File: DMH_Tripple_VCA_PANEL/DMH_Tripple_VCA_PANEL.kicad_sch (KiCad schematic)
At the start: 21 parts, among them J0 Panel_GND_Solder_Wire_Pad

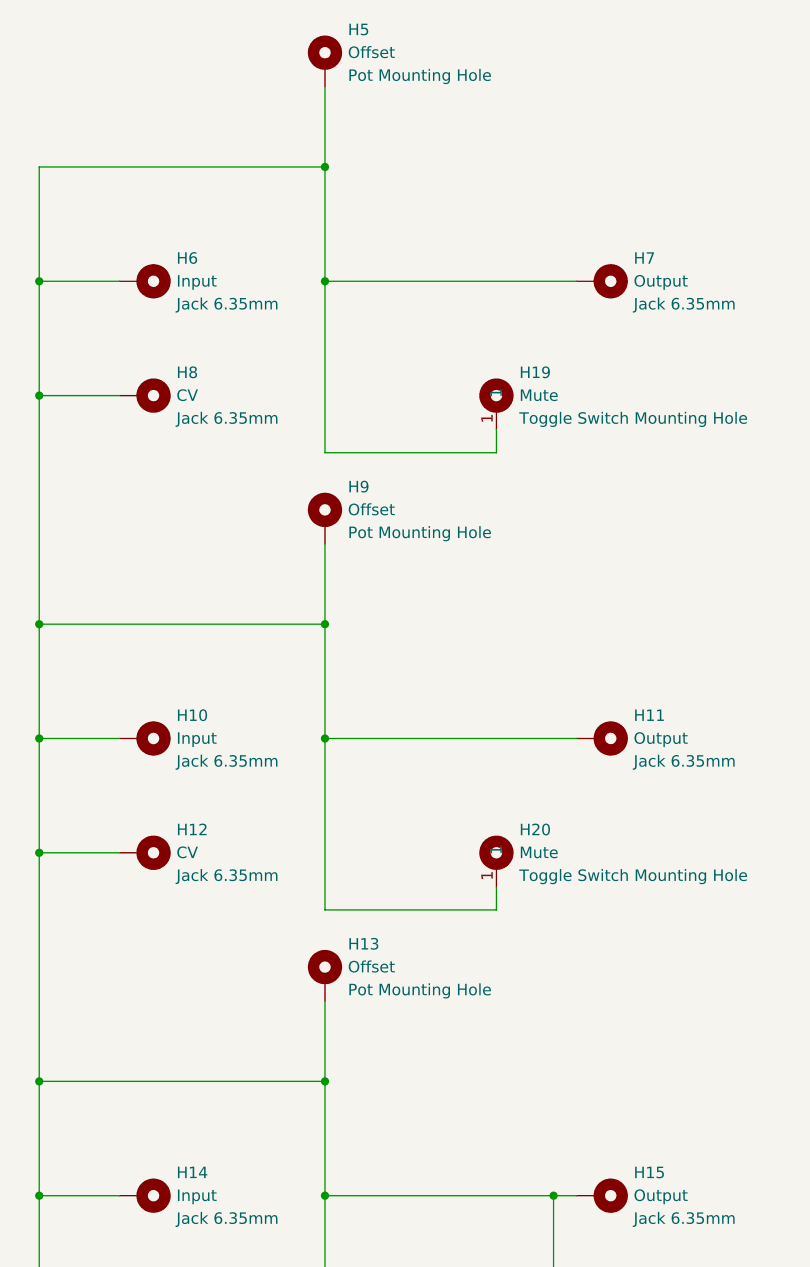
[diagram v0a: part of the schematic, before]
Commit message: Added LED holes
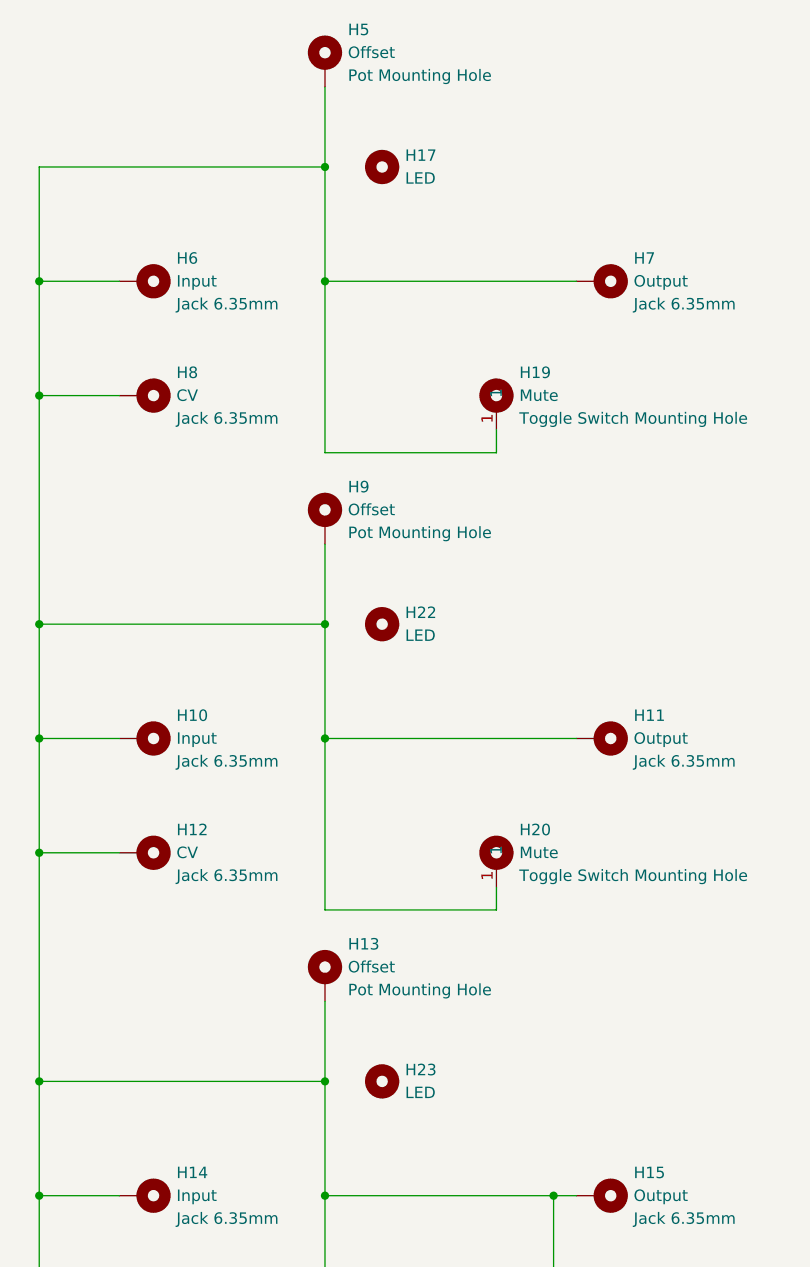
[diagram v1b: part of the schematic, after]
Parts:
- added H17, H22, H23: LED, SynthStuff:MountingHole_LED_3mm, symbol Mechanical:MountingHole
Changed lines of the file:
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@@
+	)
+	(symbol
+		(lib_id "Mechanical:MountingHole")
+		(at 88.9 114.3 0)
+		(unit 1)
+		(exclude_from_sim yes)
+		(in_bom no)
+		(on_board yes)
+		(dnp no)
+		(fields_autoplaced yes)
+		(property "Reference" "H22"
+			(at 91.44 113.0299 0)
+			(effects
+				(font
+					(size 1.27 1.27)
+				)
+				(justify left)
+			)
+		)
+		(property "Value" "LED"
+			(at 91.44 115.5699 0)
+			(effects
+				(font
+					(size 1.27 1.27)
+				)
+				(justify left)
+			)
+		)
+		(property "Footprint" "SynthStuff:MountingHole_LED_3mm"
+			(at 88.9 114.3 0)
+			(effects
+				(font
+					(size 1.27 1.27)
+				)
+				(hide yes)
+			)
+		)
+		(property "Datasheet" "~"
+			(at 88.9 114.3 0)
+			(effects
+				(font
+					(size 1.27 1.27)
+				)
+				(hide yes)
+			)
+		)
+		(property "Description" "Mounting Hole without connection"
+			(at 88.9 114.3 0)
+			(effects
+				(font
+					(size 1.27 1.27)
+				)
+				(hide yes)
+			)
+		)
+		(instances
+			(project "DMH_Tripple_VCA_PANEL"
+				(path "/a552705f-a9fe-462e-9913-5cfcc08b233c"
+					(reference "H22")
+					(unit 1)
+				)
+			)
+		)
 	)
 	(symbol
@@
 	)
 	(symbol
+		(lib_id "Mechanical:MountingHole")
+		(at 88.9 63.5 0)
+		(unit 1)
+		(exclude_from_sim yes)
+		(in_bom no)
+		(on_board yes)
+		(dnp no)
+		(fields_autoplaced yes)
+		(property "Reference" "H17"
+			(at 91.44 62.2299 0)
+			(effects
+				(font
+					(size 1.27 1.27)
+				)
+				(justify left)
+			)
+		)
+		(property "Value" "LED"
+			(at 91.44 64.7699 0)
+			(effects
+				(font
+					(size 1.27 1.27)
+				)
+				(justify left)
+			)
+		)
+		(property "Footprint" "SynthStuff:MountingHole_LED_3mm"
+			(at 88.9 63.5 0)
+			(effects
+				(font
+					(size 1.27 1.27)
+				)
+				(hide yes)
+			)
+		)
+		(property "Datasheet" "~"
+			(at 88.9 63.5 0)
+			(effects
+				(font
+					(size 1.27 1.27)
+				)
+				(hide yes)
+			)
+		)
+		(property "Description" "Mounting Hole without connection"
+			(at 88.9 63.5 0)
+			(effects
+				(font
+					(size 1.27 1.27)
+				)
+				(hide yes)
+			)
+		)
+		(instances
+			(project "DMH_Tripple_VCA_PANEL"
+				(path "/a552705f-a9fe-462e-9913-5cfcc08b233c"
+					(reference "H17")
+					(unit 1)
+				)
+			)
+		)
+	)
+	(symbol
 		(lib_id "SynthStuff:MountingHole_Rails")
 		(at 27.94 265.43 0)
@@
 					(unit 1)
 				)
+			)
+		)
+	)
+	(symbol
+		(lib_id "Mechanical:MountingHole")
+		(at 88.9 165.1 0)
+		(unit 1)
+		(exclude_from_sim yes)
+		(in_bom no)
+		(on_board yes)
+		(dnp no)
+		(fields_autoplaced yes)
+		(property "Reference" "H23"
+			(at 91.44 163.8299 0)
+			(effects
+				(font
+					(size 1.27 1.27)
+				)
+				(justify left)
+			)
+		)
+		(property "Value" "LED"
+			(at 91.44 166.3699 0)
+			(effects
+				(font
+					(size 1.27 1.27)
+				)
+				(justify left)
+			)
+		)
+		(property "Footprint" "SynthStuff:MountingHole_LED_3mm"
+			(at 88.9 165.1 0)
+			(effects
+				(font
+					(size 1.27 1.27)
+				)
+				(hide yes)
+			)
+		)
+		(property "Datasheet" "~"
+			(at 88.9 165.1 0)
+			(effects
+				(font
+					(size 1.27 1.27)
+				)
+				(hide yes)
+			)
+		)
+		(property "Description" "Mounting Hole without connection"
+			(at 88.9 165.1 0)
+			(effects
+				(font
+					(size 1.27 1.27)
+				)
+				(hide yes)
+			)
+		)
+		(instances
+			(project "DMH_Tripple_VCA_PANEL"
+				(path "/a552705f-a9fe-462e-9913-5cfcc08b233c"
+					(reference "H23")
+					(unit 1)
+				)

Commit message: Finished Schematic
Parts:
- H17, H22, H23: footprint SynthStuff:MountingHole_LED_3mm -> SynthStuff:MountingHole_LED_5mm
- H18: value Mix Out + -> Mix Out
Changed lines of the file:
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@@
 			)
 		)
-		(property "Footprint" "SynthStuff:MountingHole_LED_3mm"
+		(property "Footprint" "SynthStuff:MountingHole_LED_5mm"
 			(at 88.9 114.3 0)
 			(effects
@@
 			)
 		)
-		(property "Footprint" "SynthStuff:MountingHole_LED_3mm"
+		(property "Footprint" "SynthStuff:MountingHole_LED_5mm"
 			(at 88.9 63.5 0)
 			(effects
@@
 			)
 		)
-		(property "Footprint" "SynthStuff:MountingHole_LED_3mm"
+		(property "Footprint" "SynthStuff:MountingHole_LED_5mm"
 			(at 88.9 165.1 0)
 			(effects
@@
 			)
 		)
-		(property "Value" "Mix Out +"
+		(property "Value" "Mix Out"
 			(at 129.54 190.4999 0)
 			(effects

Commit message: Changed LEDs to bi-color
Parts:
- H17, H22, H23: footprint SynthStuff:MountingHole_LED_5mm -> SynthStuff:MountingHole_LED_3mm
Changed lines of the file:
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@@
 			)
 		)
-		(property "Footprint" "SynthStuff:MountingHole_LED_5mm"
+		(property "Footprint" "SynthStuff:MountingHole_LED_3mm"
 			(at 88.9 114.3 0)
 			(effects
@@
 			)
 		)
-		(property "Footprint" "SynthStuff:MountingHole_LED_5mm"
+		(property "Footprint" "SynthStuff:MountingHole_LED_3mm"
 			(at 88.9 63.5 0)
 			(effects
@@
 			)
 		)
-		(property "Footprint" "SynthStuff:MountingHole_LED_5mm"
+		(property "Footprint" "SynthStuff:MountingHole_LED_3mm"
 			(at 88.9 165.1 0)
 			(effects
